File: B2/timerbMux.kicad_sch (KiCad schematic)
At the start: 2 parts, among them U306 74HC08, U307 74HC153

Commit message: Almost 0.1.1
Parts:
- renumbered U307 to U218, U306 to U229
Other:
- company: (none) -> Daniel Molina
- title: (none) -> 74HCT6526 Board 2
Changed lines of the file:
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@@
 (kicad_sch (version 20211123) (generator eeschema)
   (paper "A4")
+  (title_block
+    (title "74HCT6526 Board 2")
+    (date "2022-08-17")
+    (rev "0.1")
+    (company "Daniel Molina")
+    (comment 1 "https://github.com/dmolinagarcia/74HCT6526")
+  )
   (junction (at 76.2 73.66) (diameter 0) (color 0 0 0 0)
   )
@@
   (symbol (lib_id "Custom 74xx:74HC08") (at 93.98 83.82 0) (unit 3)
     (in_bom yes) (on_board yes)
-    (property "Reference" "U306" (id 0) (at 92.71 83.82 0))
+    (property "Reference" "U229" (id 0) (at 92.71 83.82 0))
     (property "Value" "74HC08" (id 1) (at 93.98 78.8186 0))
     (property "Footprint" "Package_SO:SO-14_3.9x8.65mm_P1.27mm" (id 2) (at 93.98 83.82 0)
@@
   (symbol (lib_id "74xx:74LS153") (at 149.86 86.36 0) (unit 1)
     (in_bom yes) (on_board yes) (fields_autoplaced)
-    (property "Reference" "U307" (id 0) (at 151.8794 62.0735 0)
+    (property "Reference" "U218" (id 0) (at 151.8794 62.0735 0)
       (effects (font (size 1.27 1.27)) (justify left))
     )

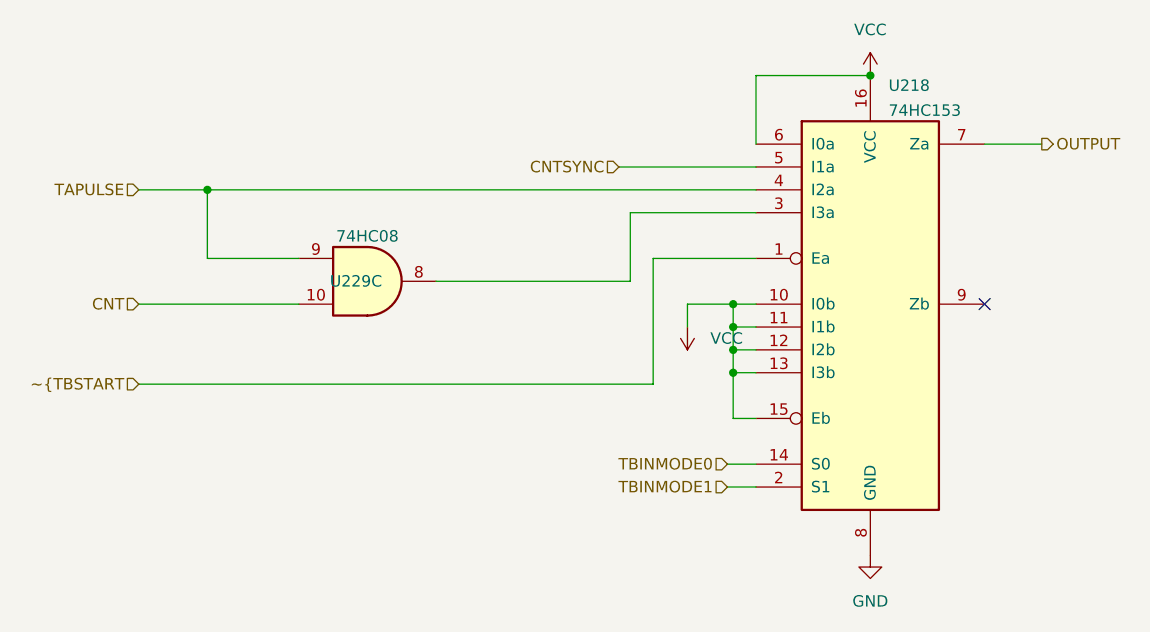
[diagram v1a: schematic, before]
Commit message: Added ICR. B2 fixes
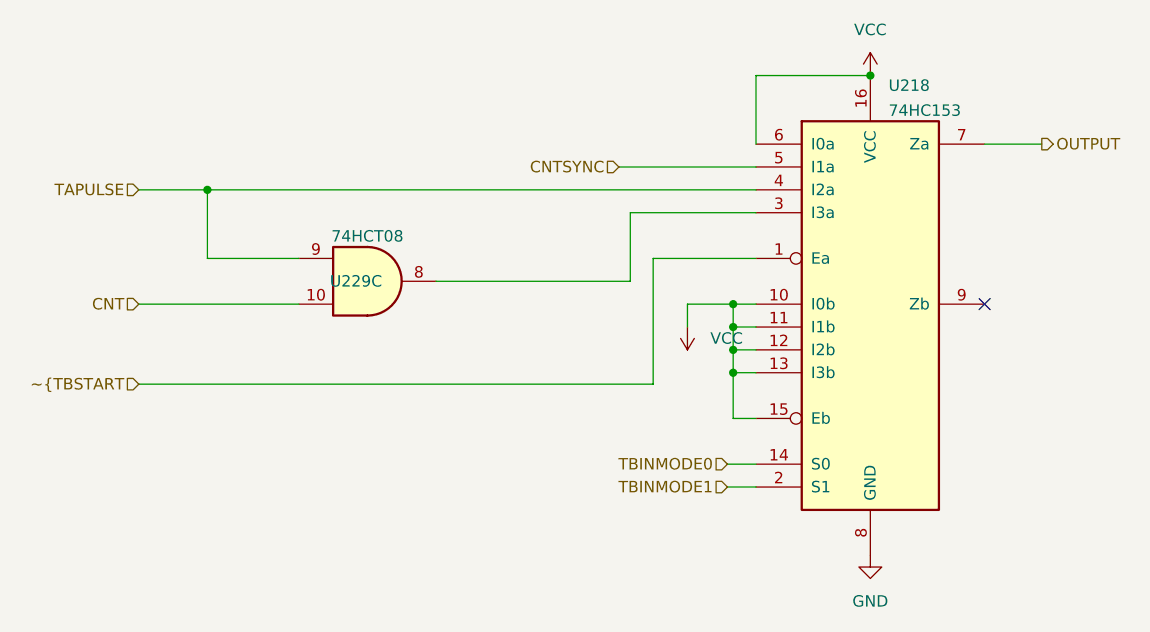
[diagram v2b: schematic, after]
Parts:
- U229: value 74HC08 -> 74HCT08
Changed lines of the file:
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@@
     (in_bom yes) (on_board yes)
     (property "Reference" "U229" (id 0) (at 92.71 83.82 0))
-    (property "Value" "74HC08" (id 1) (at 93.98 78.8186 0))
+    (property "Value" "74HCT08" (id 1) (at 93.98 78.8186 0))
     (property "Footprint" "Package_SO:SO-14_3.9x8.65mm_P1.27mm" (id 2) (at 93.98 83.82 0)
       (effects (font (size 1.27 1.27)) hide)
